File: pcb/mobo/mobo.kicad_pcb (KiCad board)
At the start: 2 copper layers, 51.6 x 89 mm, 76 parts, among them J1 ISP, J2 PEEL_MOTOR, J3 DRIVE_MOTOR, J5 SPRING_FINGERS, J8 USART1, U1 ATmega328PB-A, U2 ATmega328PB-M, U3 LED_RGB, U4 AP1117-50, U5 MC34063AD, U6 SP308xE, U7 DRV8837, U8 DRV8837, Y1 16MHz

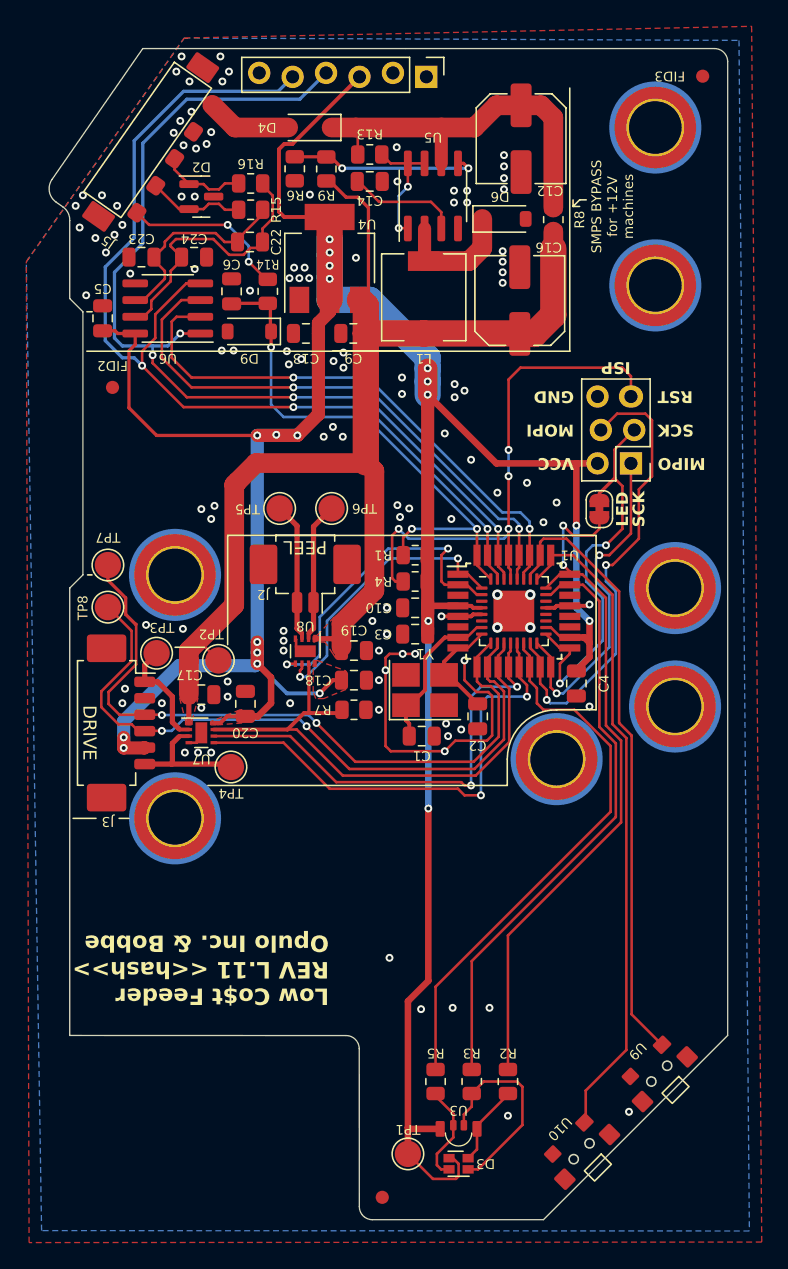
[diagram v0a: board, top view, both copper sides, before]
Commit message: Add keepout area for counter sinks to mounting holes
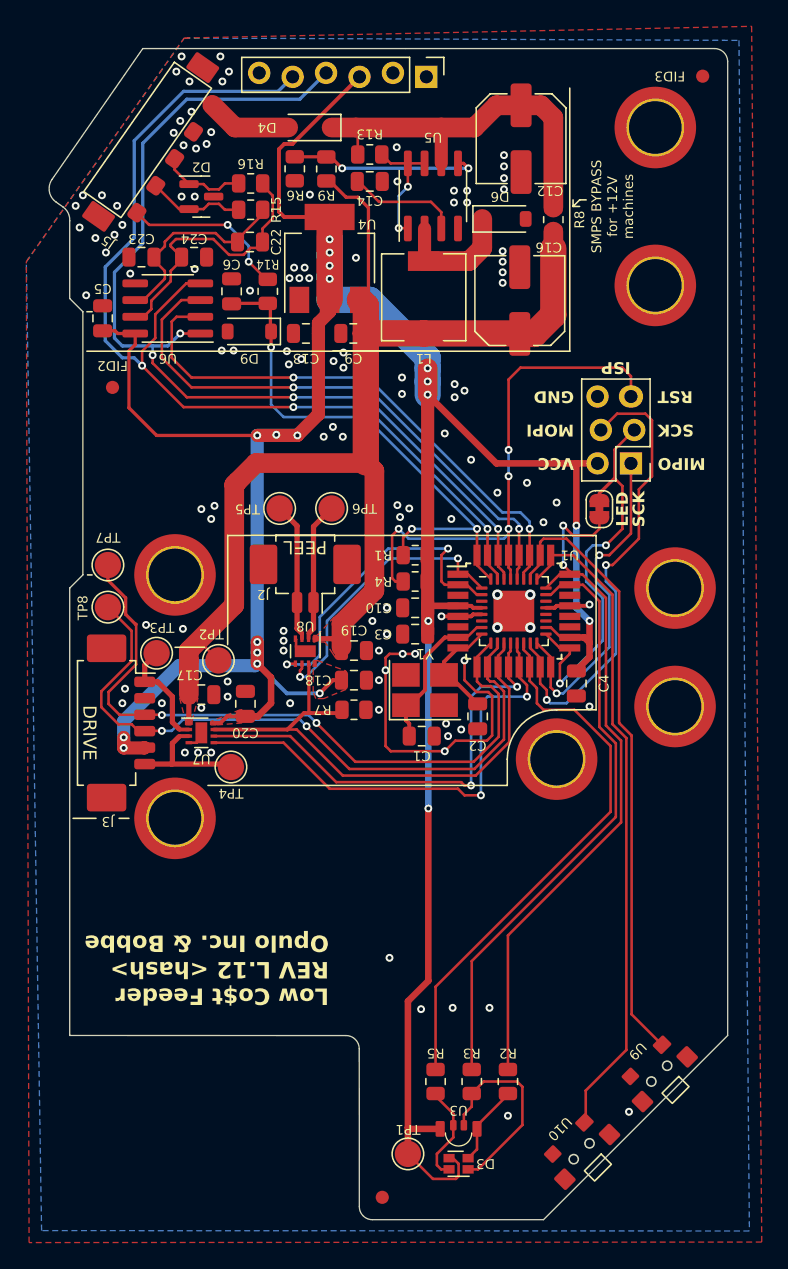
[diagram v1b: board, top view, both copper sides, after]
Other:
- board text added: "Low Co$t Feeder REV L.12 <hash> Opulo Inc. & Bobbe"
- board text removed: "Low Co$t Feeder REV L.11 <<hash>> Opulo Inc. & Bobbe"
